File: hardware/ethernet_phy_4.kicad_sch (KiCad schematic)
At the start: 29 parts, among them J3 RJMG1S8008101BR, SW2 SW TACT-SPST, U2 DP83826IRHBR, Y2 ABM8G-25.000MHZ-9-B4Y-T

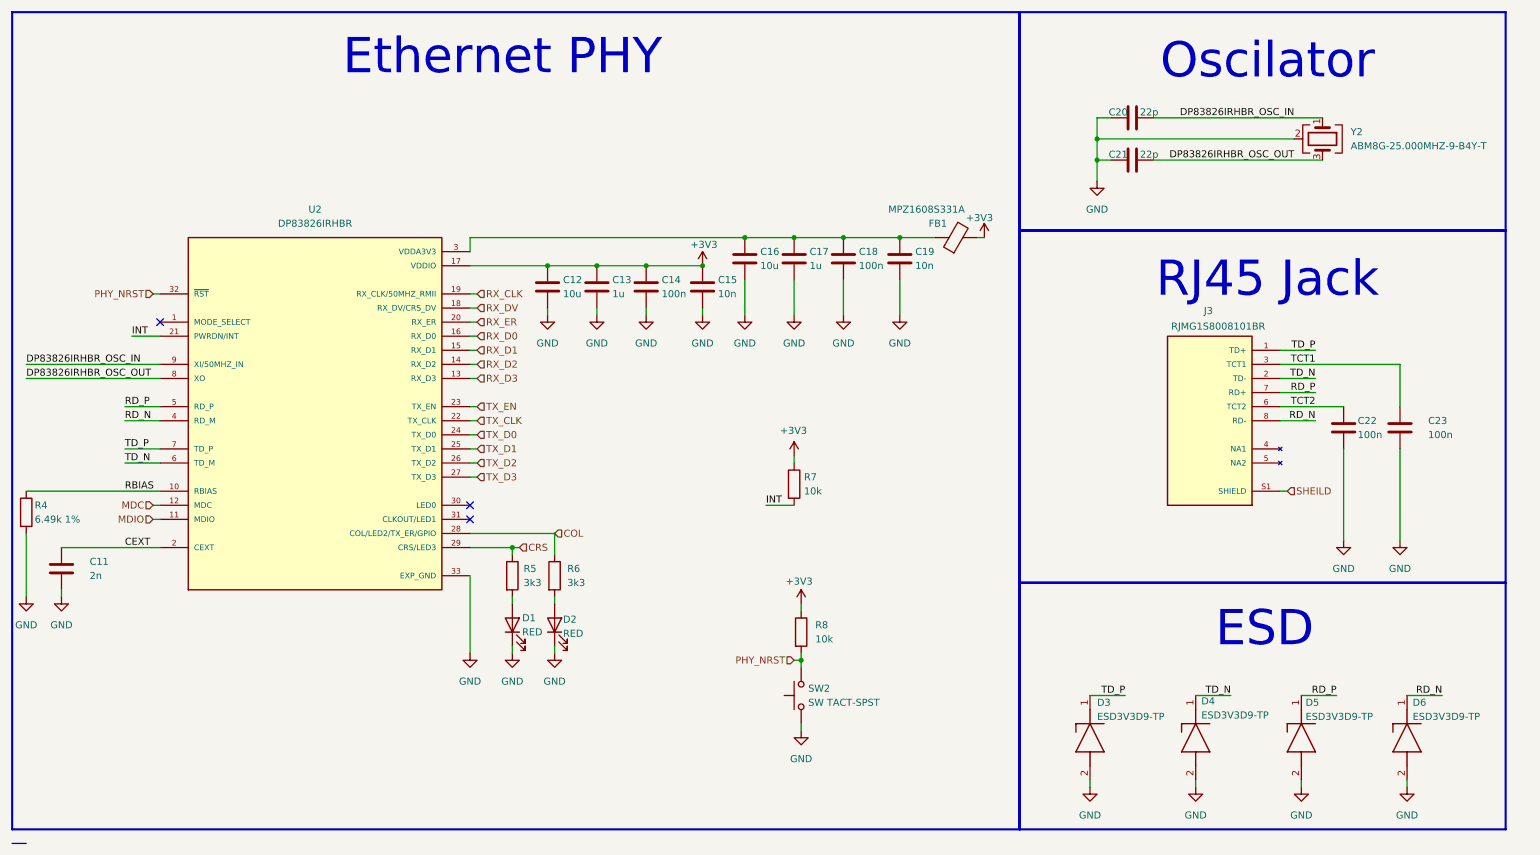
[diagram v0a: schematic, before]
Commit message: Route Ethernet section and add global labels
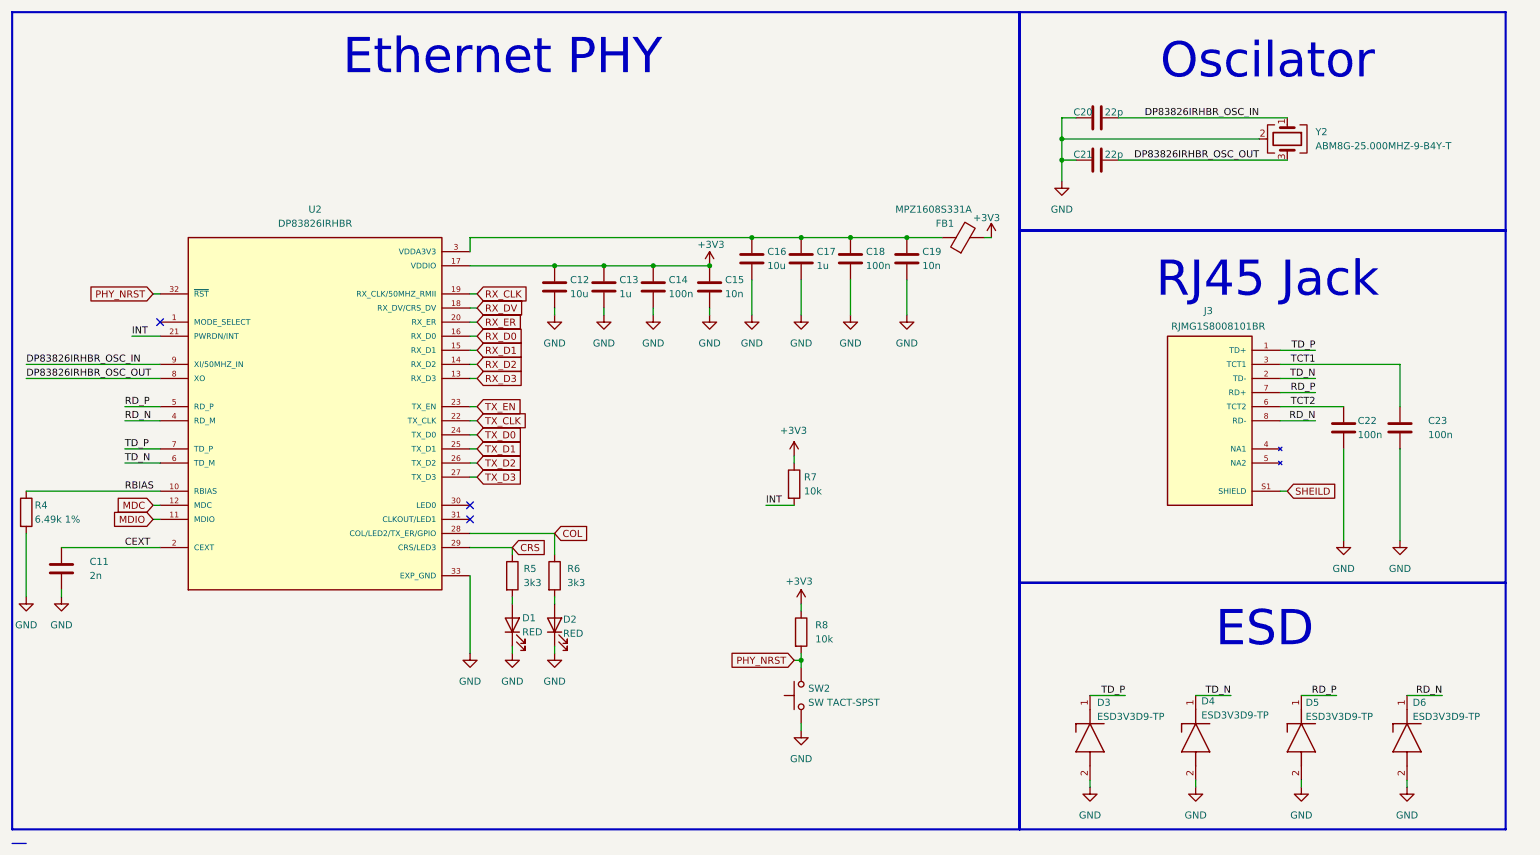
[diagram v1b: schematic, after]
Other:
- moved on the sheet: C12, C13, C14, C15, C16, C17, C18, C19, C20, C21, FB1, Y2

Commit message: Add prices to BOM
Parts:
- R5, R6: value 3k3 -> 3.3k
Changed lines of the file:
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@@
 			)
 		)
-		(property "Value" "3k3"
+		(property "Value" "3.3k"
 			(at 107.442 119.38 0)
 			(show_name no)
@@
 			)
 		)
-		(property "Value" "3k3"
+		(property "Value" "3.3k"
 			(at 115.316 119.38 0)
 			(show_name no)
